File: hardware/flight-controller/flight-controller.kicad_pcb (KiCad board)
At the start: 2 copper layers, 66.5 x 77.5 mm, 130 parts, among them J1 XT-60, J10 IDC-10, J2 Conn_01x05, J3 IDC-10, J4 Conn_01x03, J5 Conn_01x03, J6 Conn_01x03, J7 IDC-10, J8 XT-60, J9 Conn_01x03, Q1 IRFR5305, Q2 S8550, SW1 SW_Push_SPDT, U1 INA226, U2 LM1117MP-3.3, U3 VL14340, U4 ESP-12E, U5 STM32U535RET6, U6 HMC5883L, U7 MPU-6050, U8 BMP280, U9 HX711, Y1 8MHz

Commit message: Mouser
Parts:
- removed L10, L2, L3, L4, L5, L6, L7, L8, L9: 2.2u/1A, Inductor_SMD:L_0603_1608Metric
- added C40: 100n, Capacitor_SMD:C_0603_1608Metric, B.Cu at (170.2, 78.7)
- added C45: 100n, Capacitor_SMD:C_0603_1608Metric, B.Cu at (170.2, 81.2)
- added C46: 100n, Capacitor_SMD:C_0603_1608Metric, B.Cu at (174.5, 80.7)
- added C51: 100n, Capacitor_SMD:C_0603_1608Metric, B.Cu at (174.5, 83.2)
- added C52: 100n, Capacitor_SMD:C_0603_1608Metric, B.Cu at (180.5, 85.0)
- added C57: 100n, Capacitor_SMD:C_0603_1608Metric, B.Cu at (180.5, 87.5)
- added C58: 100n, Capacitor_SMD:C_0603_1608Metric, B.Cu at (184.0, 89.7)
- added C61: 100n, Capacitor_SMD:C_0603_1608Metric, B.Cu at (184.0, 92.2)
- added C64: 100n, Capacitor_SMD:C_0603_1608Metric, B.Cu at (184.8, 95.2)
- renumbered C40 to C42, C42 to C43, C43 to C44, C44 to C47, C45 to C48, C46 to C49, C47 to C50, C48 to C53, C49 to C54, C50 to C55, C51 to C56, C52 to C59, C53 to C60, C54 to C62, C55 to C63, C56 to C65, C57 to C66
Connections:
- C42 pad 1: /connectors/FLOW_5V -> +5V
- C44 pad 1: /connectors/SERVO1_5V -> +5V
- C47 pad 1: /connectors/FLOW_3V3 -> +3.3V
- C50 pad 1: /connectors/SERVO2_5V -> +5V
- C53 pad 1: /connectors/RANGE_5V -> +5V
- C56 pad 1: /connectors/SERVO3_5V -> +5V
- C59 pad 1: /connectors/RANGE_3V3 -> +3.3V
- C62 pad 1: /connectors/GPS_TACHO_LOAD_5V -> +5V
- C65 pad 1: /connectors/GPS_TACHO_LOAD_3V3 -> +3.3V
- J10 pad 2: /connectors/GPS_TACHO_LOAD_5V -> +5V
- J10 pad 4: /connectors/GPS_TACHO_LOAD_3V3 -> +3.3V
- J3 pad 2: /connectors/FLOW_5V -> +5V
- J3 pad 4: /connectors/FLOW_3V3 -> +3.3V
- J4 pad 2: /connectors/SERVO1_5V -> +5V
- J5 pad 2: /connectors/SERVO2_5V -> +5V
- J6 pad 2: /connectors/SERVO3_5V -> +5V
- J7 pad 2: /connectors/RANGE_5V -> +5V
- J7 pad 4: /connectors/RANGE_3V3 -> +3.3V

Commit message: routing: first blood
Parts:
- C2, C43, C44, C47, C48, C49, C50, C56, C59, C60, C62, C63, R10, R3, R30, R31, R4, R6: moved to B.Cu
- moved R16 112.5 mm to (250.6, 132.0)
- moved R17 112.5 mm to (250.6, 134.5)
- moved R18 112.5 mm to (250.6, 137.0)
- moved R19 112.5 mm to (250.6, 139.5)
- moved R20 112.5 mm to (250.6, 142.0)
- moved R21 112.5 mm to (250.6, 144.5)
- moved D2 105.5 mm to (254.6, 139.5)
- moved R11 105.3 mm to (246.8, 134.5)
- moved R12 105.3 mm to (246.8, 137.0)
- moved R14 105.3 mm to (246.8, 142.0)
- moved R15 105.3 mm to (246.8, 144.5)
- moved C24 105.3 mm to (246.8, 132.0)
- moved R13 105.3 mm to (246.8, 139.5)
- moved D3 99.6 mm to (254.4, 131.8)
- moved D4 99.6 mm to (254.4, 134.4)
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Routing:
- added copper zone on In1.Cu, net +3.3V
- added copper zone on F.Cu, net +5V
- added copper zone on F.Cu, net /power/BATTERY_IN
- added copper zone on B.Cu, net GND
- added copper zone on F.Cu, net GND
- added copper zone on In2.Cu, net GND
- added copper zone on F.Cu, net Net-(D1-K)
- added copper zone on F.Cu, net Net-(Q1-D)
- added copper zone on F.Cu, net VBUS
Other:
- board size 66.5 x 77.5 mm -> 66.7 x 75.4 mm
- copper layers 2 -> 4

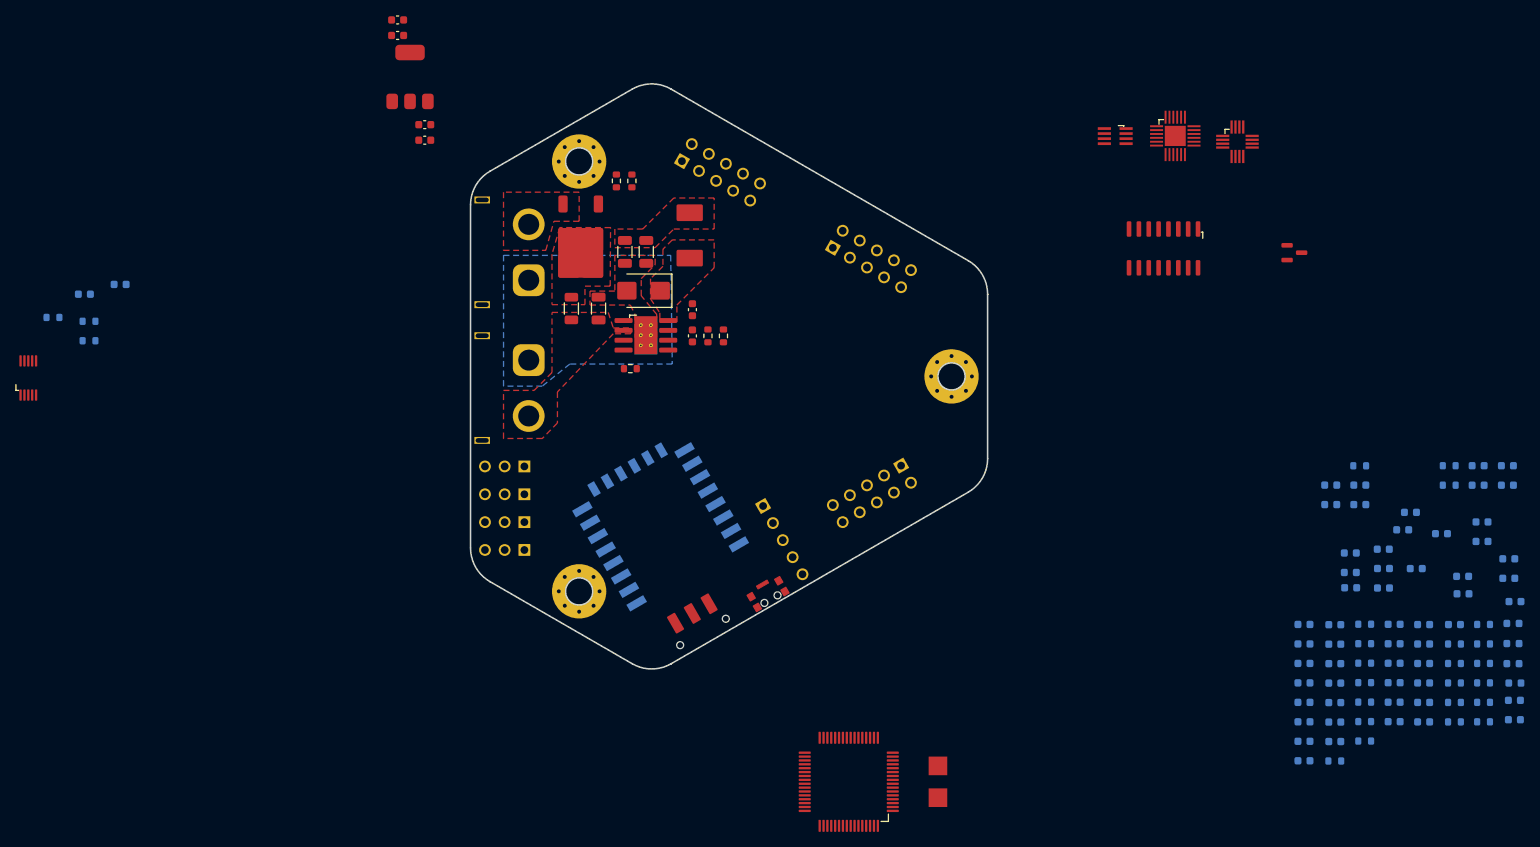
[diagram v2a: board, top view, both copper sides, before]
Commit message: routing: rought placement
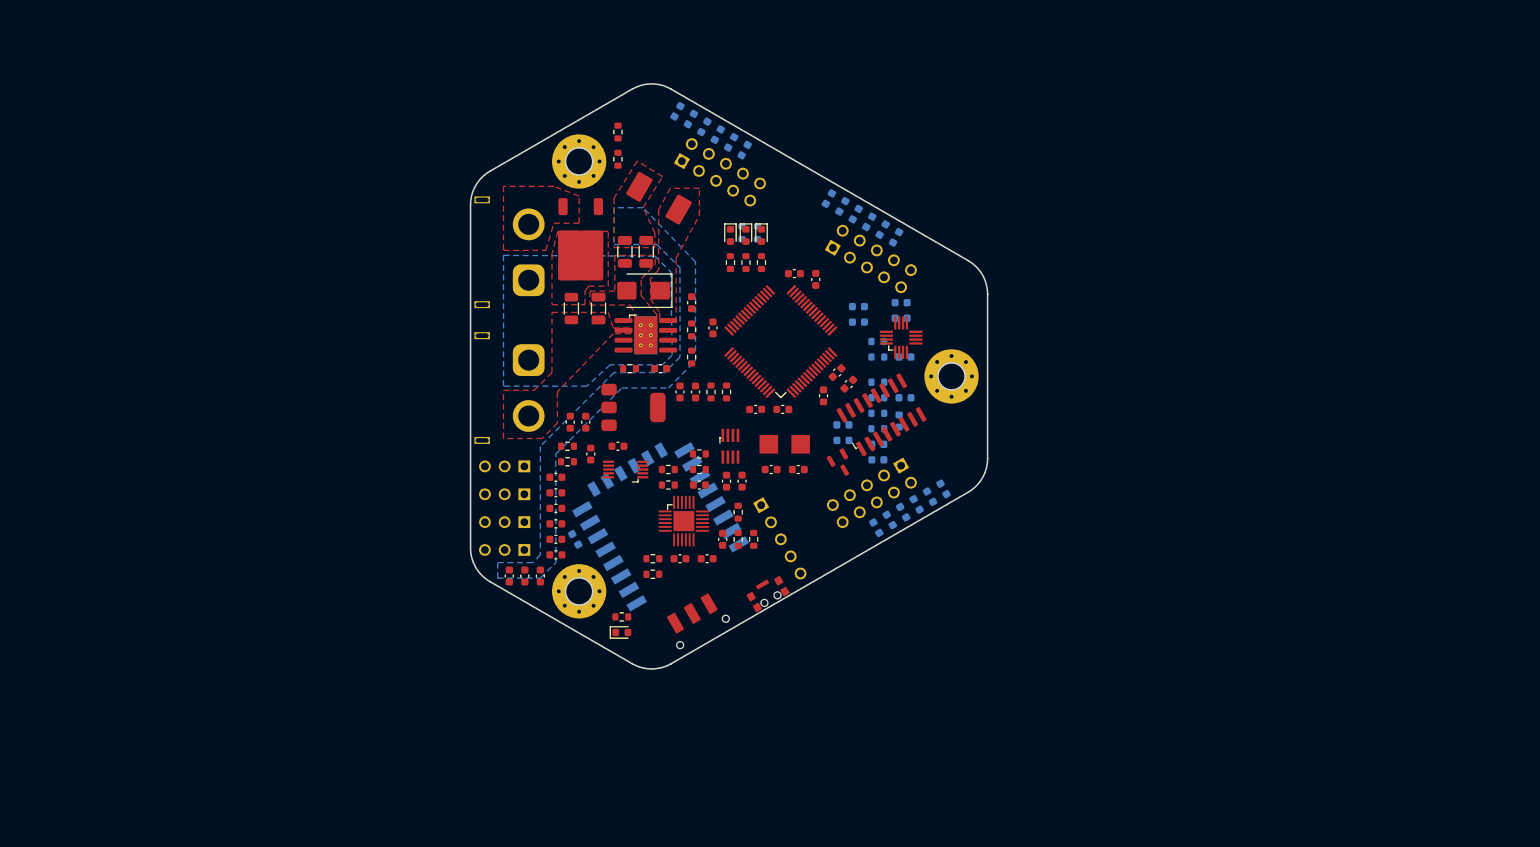
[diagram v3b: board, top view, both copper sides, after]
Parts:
- C1, C14, C15, C16, C17, C19, C2, C20, C21, C22, C23, C24, C26, C27, C28, C29, C32, C33, C43, C44, C45, C49, C50, C51, C55, C56, C57, D2, D3, D4, D5, R10, R11, R12, R13, R14, R15, R16, R17, R18, R19, R20, R21, R22, R23, R3, R4, R6: moved to F.Cu
- moved C57 119.7 mm to (131.0, 113.0), turned to 0 degrees
- moved C50 117.1 mm to (131.0, 121.0), turned to 0 degrees
- moved C49 117.1 mm to (131.0, 119.0), turned to 0 degrees
- moved C52 116.4 mm to (146.7, 65.8), turned to 60 degrees
- moved D2 115.3 mm to (139.5, 133.0), turned to 0 degrees
- moved D5 115.0 mm to (153.5, 81.8), turned to -90 degrees
- moved C55 114.2 mm to (131.0, 117.0), turned to 0 degrees
- moved D4 112.0 mm to (155.5, 81.8), turned to -90 degrees
- moved C58 111.7 mm to (155.3, 70.8), turned to 60 degrees
- moved R19 111.2 mm to (153.5, 85.3), turned to 90 degrees
- moved C18 109.9 mm to (133.5, 121.0), turned to -60 degrees
- moved D3 109.0 mm to (157.5, 81.8), turned to -90 degrees
- moved R21 108.3 mm to (151.0, 102.0), turned to -90 degrees
- moved R18 108.2 mm to (155.5, 85.3), turned to 90 degrees
- moved C60 107.9 mm to (151.9, 68.8), turned to 60 degrees
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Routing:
- added copper zone on B.Cu, net +5V

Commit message: routing: all signals routed
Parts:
- C12, C13, C25, C34, C35: moved to F.Cu
- D1: value ~ -> SK56
- R20, R21: moved to B.Cu
- R30: renamed from R31; value 4k7 -> 4.7k
- R31: renamed from R30; value 4k7 -> 4.7k
- SW1: value SW_Push_SPDT -> JS102011SAQN
- SW2: value ~ -> KMS231GPLFS
- U3: value VL14340 -> LV14340
- moved U8 18.2 mm to (137.0, 116.8), turned to 180 degrees
- moved J2 17.0 mm to (142.7, 125.1)
- moved C28 14.4 mm to (140.8, 115.5), turned to 90 degrees
- moved R27 13.8 mm to (166.8, 113.2), turned to 180 degrees
- moved R21 13.7 mm to (162.8, 95.0)
- moved C29 13.4 mm to (140.8, 119.0), turned to 90 degrees
- moved R16 13.3 mm to (152.2, 123.0)
- moved R31 13.2 mm to (160.0, 93.8), turned to 180 degrees
- moved C43 11.3 mm to (129.2, 115.2), turned to 90 degrees
- moved C44 11.3 mm to (131.2, 115.2), turned to 90 degrees
- moved C45 11.3 mm to (133.2, 115.2), turned to 90 degrees
- moved R30 10.7 mm to (160.0, 91.8), turned to 180 degrees
- moved R26 10.3 mm to (166.8, 111.2)
- moved R13 9.51 mm to (143.0, 133.0), turned to 0 degrees
- moved R14 9.51 mm to (143.0, 135.0), turned to 0 degrees
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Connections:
- J10 pad 5: GND -> LOAD_SN
- J10 pad 6: GPS_TXD -> GND
- J10 pad 9: LOAD_SN -> GPS_TXD
- J3 pad 1: FLOW_SCK -> SPARE_UART_TX
- J3 pad 3: FLOW_MISO -> SPARE_UART_RX
- J3 pad 7: SPARE_UART_RX -> FLOW_SCK
- J3 pad 8: FLOW_CS -> FLOW_MISO
- J3 pad 9: SPARE_UART_TX -> FLOW_CS
- J7 pad 1: SPARE_I2C_SDA -> RANGE_TRIG
- J7 pad 3: SPARE_I2C_SCL -> RANGE_ECHO
- J7 pad 6: RANGE_ECHO -> SPARE_I2C_SDA
- J7 pad 8: RANGE_TRIG -> SPARE_I2C_SCL
- U5 pad 26: /microcontroller/LED_R -> unconnected-(U5-PB0-Pad26)
- U5 pad 33: unconnected-(U5-PB12-Pad33) -> /microcontroller/LED_R
- U5 pad 38: PWR_INT -> unconnected-(U5-PC7-Pad38)
- U5 pad 41: SERVO1 -> SERVO3
- U5 pad 43: SERVO3 -> SERVO1
- U5 pad 50: unconnected-(U5-PA15-Pad50) -> IMU_INT
- U5 pad 51: GPS_RXD -> /microcontroller/ESP_RXD
- U5 pad 52: GPS_TXD -> /microcontroller/ESP_TXD
- U5 pad 53: /microcontroller/ESP_RXD -> GPS_RXD
- U5 pad 54: /microcontroller/ESP_TXD -> GPS_TXD
- U5 pad 57: IMU_INT -> PWR_INT
- U5 pad 58: IMU_SCL -> MISC_SCL
- U5 pad 59: IMU_SDA -> MISC_SDA
- U5 pad 61: MISC_SCL -> IMU_SCL
- U5 pad 62: MISC_SDA -> IMU_SDA
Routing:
- net GND: track 0.00 -> 190.6 mm, vias 0 -> 114
- net +3.3V: track 0.00 -> 175.3 mm, vias 0 -> 51
- net +5V: track 0.00 -> 150.9 mm, vias 0 -> 44
- net Net-(SW1-B): track 0.00 -> 75.2 mm, vias 0 -> 4
- net /microcontroller/RESET: track 0.00 -> 71.9 mm, vias 0 -> 4
- net SERVO3: track 0.00 -> 54.3 mm, vias 0 -> 2
- net SERVO2: track 0.00 -> 53.6 mm, vias 0 -> 2
- net SERVO1: track 0.00 -> 50.1 mm, vias 0 -> 2
- net /microcontroller/SWDIO: track 0.00 -> 47.8 mm, vias 0 -> 2
- net ESC: track 0.00 -> 46.9 mm, vias 0 -> 2
- net /microcontroller/SWCLK: track 0.00 -> 44.5 mm, vias 0 -> 2
- net MISC_SDA: track 0.00 -> 40.4 mm, vias 0 -> 1
- net /microcontroller/ESP_TXD: track 0.00 -> 40.3 mm, vias 0 -> 1
- net /microcontroller/ESP_RXD: track 0.00 -> 39.2 mm, vias 0 -> 1
- net IMU_INT: track 0.00 -> 37.9 mm, vias 0 -> 2
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
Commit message: routing: silkscreen
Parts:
- added G***: LOGO, LOGO, F.Cu at (134.2, 97.5)
- added G***: LOGO, LOGO, F.Cu at (181.6, 107.0)
- added G***: LOGO, LOGO, B.Cu at (149.8, 105.0)
- added G***: LOGO, LOGO, B.Cu at (140.0, 87.9)
- moved R10 2.00 mm to (139.5, 133.0), turned to 0 degrees
- moved D2 2.00 mm to (139.5, 131.0), turned to 0 degrees
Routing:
- net /microcontroller/ESP_EN: track 1.70 -> 0.37 mm
- net GND: track 190.6 -> 190.0 mm
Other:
- board text added: "3V3"
- board text added: "5V"
- board text added: "BATTERY"
- board text added: "CS"
- board text added: "E+"
- board text added: "E-"
- board text added: "ECHO"
- board text added: "ESC"
- board text added: "FLOW"
- board text added: "GND"
- board text added: "INT"
- board text added: "JLCJLCJLCJLC"
- board text added: "MISO"
- board text added: "MOSI"
- board text added: "NC"
- board text added: "ON 0FF"
- board text added: "PA1"
- board text added: "PA2"
- board text added: "PA3"
- board text added: "PWM"
- board text added: "PWR"
- board text added: "RANGE"
- board text added: "RESET"
- board text added: "RX"
- board text added: "S+"
- board text added: "S-"
- board text added: "SCK"
- board text added: "SCL"
- board text added: "SDA"
- board text added: "SERVOS"
- board text added: "SWCLK"
- board text added: "SWD"
- board text added: "SWDIO"
- board text added: "TACH"
- board text added: "TACH LOAD GPS"
- board text added: "TRIG"
- board text added: "TX"
- board text added: "UAV TVC Goose II Flight Controller V2.1 by Eryk Możdżeń August 2024"
- board text added: "X"
- board text added: "Y"
- board text added: "Z"

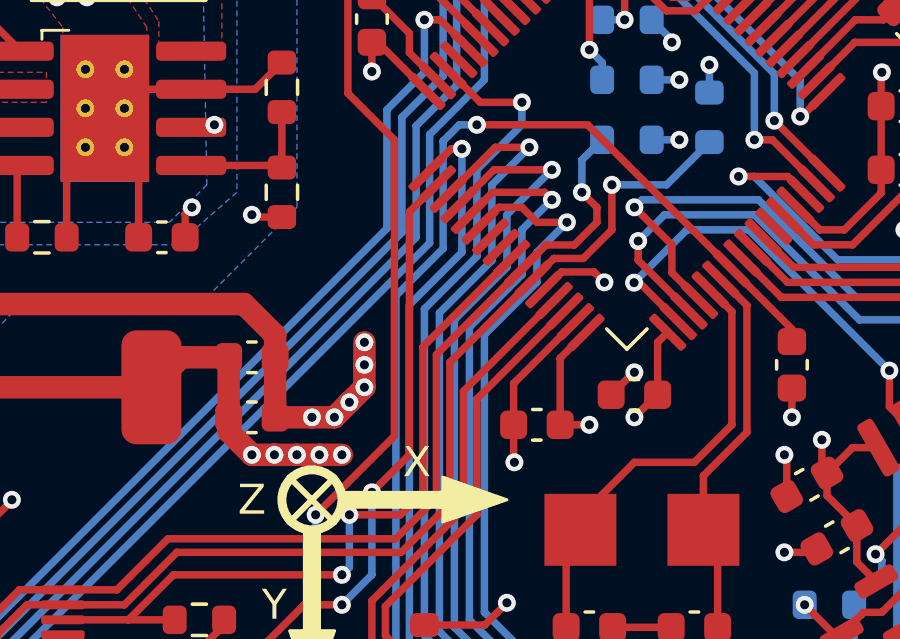
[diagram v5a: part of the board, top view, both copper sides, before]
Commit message: fix IMU interrupt
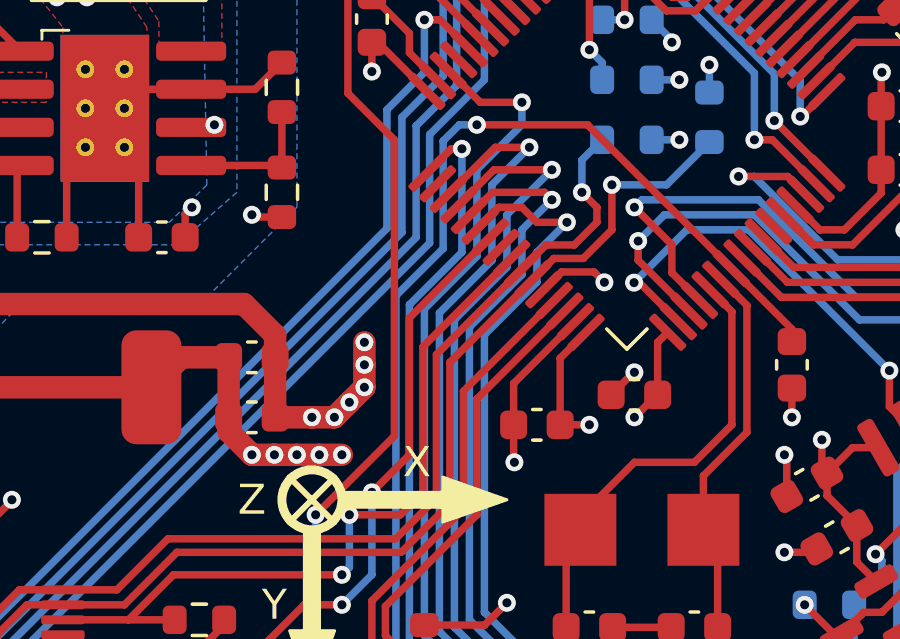
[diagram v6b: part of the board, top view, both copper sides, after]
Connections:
- U5 pad 50: IMU_INT -> unconnected-(U5-PA15-Pad50)
- U5 pad 55: unconnected-(U5-PB3-Pad55) -> IMU_INT
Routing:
- net IMU_INT: track 37.9 -> 36.9 mm
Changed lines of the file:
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@@
 	(net 102 "unconnected-(U5-PC3-Pad11)")
 	(net 103 "unconnected-(U5-PC7-Pad38)")
-	(net 104 "unconnected-(U5-PB3-Pad55)")
+	(net 104 "unconnected-(U5-PA15-Pad50)")
 	(net 105 "unconnected-(U5-PB4-Pad56)")
 	(net 106 "unconnected-(U7-NC-Pad15)")
@@
 		(tags "resistor")
 		(property "Reference" "R2"
-			(at 0.000001 -1.429999 360)
+			(at 0.000001 -1.429999 0)
 			(layer "F.SilkS")
 			(hide yes)
@@
 		)
 		(property "Value" "10k"
-			(at -72.515 20.17 360)
+			(at -72.515 20.17 0)
 			(layer "F.Fab")
 			(effects
@@
 		)
 		(fp_text user "${REFERENCE}"
-			(at 0 0 360)
+			(at 0 0 0)
 			(layer "F.Fab")
 			(effects
@@
 		(tags "capacitor")
 		(property "Reference" "C7"
-			(at 0.000001 -1.429999 360)
+			(at 0.000001 -1.429999 0)
 			(layer "F.SilkS")
 			(hide yes)
@@
 		)
 		(property "Value" "100n"
-			(at -0.000001 1.429999 360)
+			(at -0.000001 1.429999 0)
 			(layer "F.Fab")
 			(effects
@@
 		)
 		(fp_text user "${REFERENCE}"
-			(at 0 0 360)
+			(at 0 0 0)
 			(layer "F.Fab")
 			(effects
@@
 		(tags "capacitor")
 		(property "Reference" "C6"
-			(at 0.000001 -1.429999 360)
+			(at 0.000001 -1.429999 0)
 			(layer "F.SilkS")
 			(hide yes)
@@
 		)
 		(property "Value" "4.7u"
-			(at -0.000001 1.429999 360)
+			(at -0.000001 1.429999 0)
 			(layer "F.Fab")
 			(effects
@@
 		)
 		(fp_text user "${REFERENCE}"
-			(at 0 0 360)
+			(at 0 0 0)
 			(layer "F.Fab")
 			(effects
@@
 			(layers "F.Cu" "F.Paste" "F.Mask")
 			(roundrect_rratio 0.25)
-			(net 101 "IMU_INT")
+			(net 104 "unconnected-(U5-PA15-Pad50)")
 			(pinfunction "PA15")
-			(pintype "bidirectional")
+			(pintype "bidirectional+no_connect")
 		)
 		(pad "51" smd roundrect
@@
 			(layers "F.Cu" "F.Paste" "F.Mask")
 			(roundrect_rratio 0.25)
-			(net 104 "unconnected-(U5-PB3-Pad55)")
+			(net 101 "IMU_INT")
 			(pinfunction "PB3")
-			(pintype "bidirectional+no_connect")
+			(pintype "bidirectional")
 		)
 		(pad "56" smd roundrect
@@
 		(tags "LED")
 		(property "Reference" "D2"
-			(at 0 -1.43 360)
+			(at 0 -1.43 0)
 			(layer "F.SilkS")
 			(hide yes)
@@
 		)
 		(property "Value" "RED"
-			(at 0 1.43 360)
+			(at 0 1.43 0)
 			(layer "F.Fab")
 			(effects
@@
 		)
 		(fp_text user "${REFERENCE}"
-			(at 0 0 360)
+			(at 0 0 0)
 			(layer "F.Fab")
 			(effects
@@
 		(tags "resistor")
 		(property "Reference" "R5"
-			(at 0.000001 -1.429999 360)
+			(at 0.000001 -1.429999 0)
 			(layer "F.SilkS")
 			(hide yes)
@@
 		)
 		(property "Value" "1k"
-			(at -0.000001 1.429999 360)
+			(at -0.000001 1.429999 0)
 			(layer "F.Fab")
 			(effects
@@
 		)
 		(fp_text user "${REFERENCE}"
-			(at 0 0 360)
+			(at 0 0 0)
 			(layer "F.Fab")
 			(effects
@@
 		(tags "resistor")
 		(property "Reference" "R10"
-			(at 0 -1.429998 360)
+			(at 0 -1.429998 0)
 			(layer "F.SilkS")
 			(hide yes)
@@
 		)
 		(property "Value" "1k"
-			(at 0 1.429998 360)
+			(at 0 1.429998 0)
 			(layer "F.Fab")
 			(effects
@@
 		)
 		(fp_text user "${REFERENCE}"
-			(at 0 0 360)
+			(at 0 0 0)
 			(layer "F.Fab")
 			(effects
@@
 	)
 	(segment
+		(start 152.75 106.25)
+		(end 152.75 101.68934)
+		(width 0.25)
+		(layer "F.Cu")
+		(net 101)
+	)
+	(segment
 		(start 145.25 121.75)
 		(end 146.0875 120.9125)
@@
 	)
 	(segment
-		(start 152.75 106.25)
-		(end 152.75 98.153806)
+		(start 143.232974 113.5)
+		(end 142 114.732974)
 		(width 0.25)
 		(layer "F.Cu")
@@
 	)
 	(segment
-		(start 143.232974 113.5)
-		(end 142 114.732974)
+		(start 152.75 101.68934)
+		(end 155.456839 98.982501)
 		(width 0.25)
 		(layer "F.Cu")
@@
 		(width 0.25)
 		(layer "F.Cu")
-		(net 101)
-	)
-	(segment
-		(start 152.75 98.153806)
-		(end 153.689072 97.214734)
-		(width 0.25)
-		(layer "F.Cu")
